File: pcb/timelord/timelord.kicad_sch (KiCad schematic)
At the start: 16 parts, among them J1 Raspberry_Pi_4, J2 OLED, J3 SMA, J4 EXTERNAL, U1 NEO-F10T

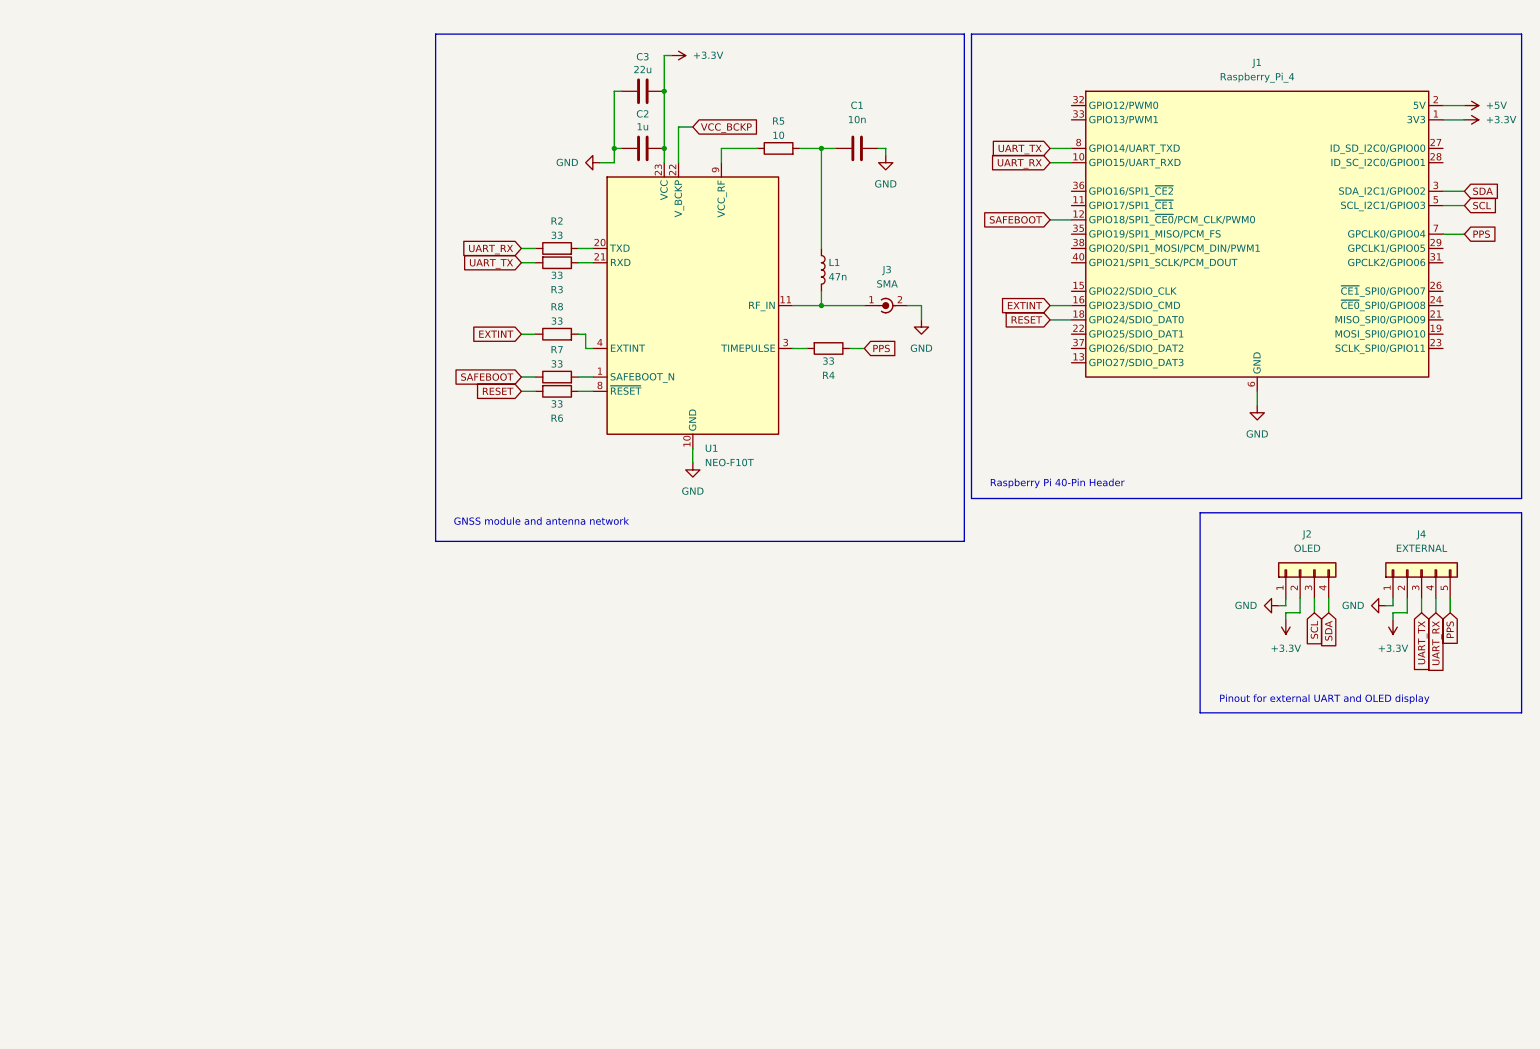
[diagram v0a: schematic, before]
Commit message: Add external I2C RTC
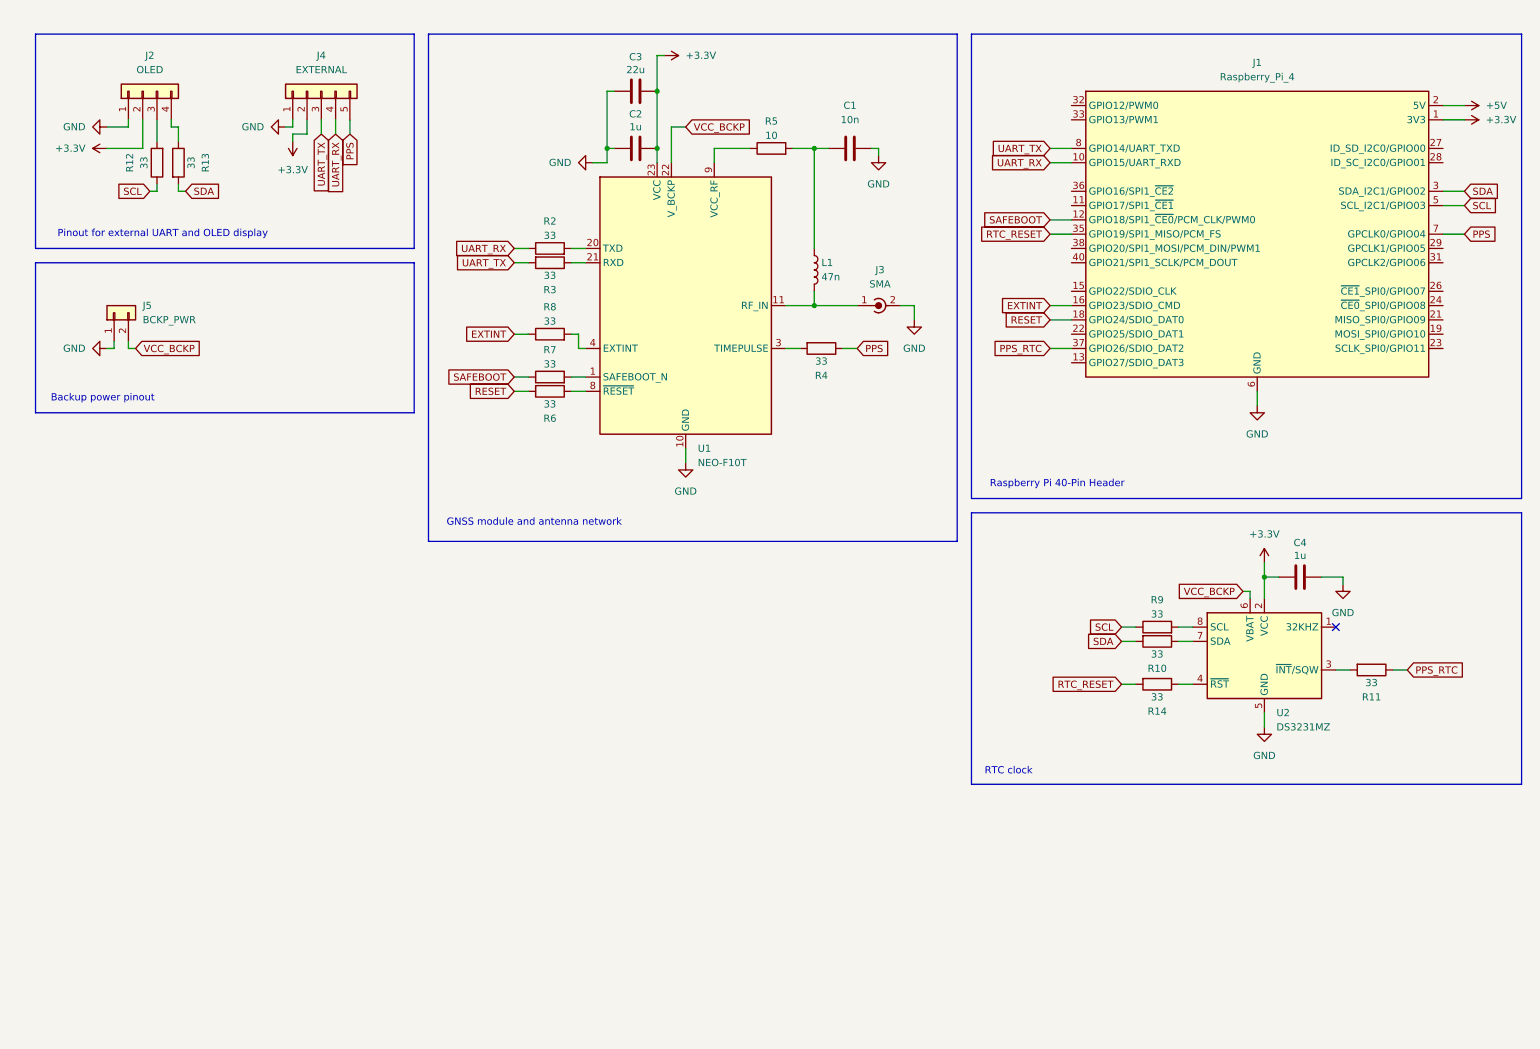
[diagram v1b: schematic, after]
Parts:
- added C4: 1u, Capacitor_SMD:C_0603_1608Metric, symbol Device:C
- added J5: BCKP_PWR, Connector_PinHeader_2.54mm:PinHeader_1x02_P2.54mm_Vertical, symbol Connector_Generic:Conn_01x02
- added R10, R11, R12, R13, R14, R9: 33, Resistor_SMD:R_0603_1608Metric, symbol Device:R
- added U2: DS3231MZ, Package_SO:SOIC-8_3.9x4.9mm_P1.27mm, symbol Timer_RTC:DS3231MZ
- J1: MFR (none) -> 485-2822
- U1: MFR (none) -> 377-NEO-F10T-00B
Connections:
- net +3.3V: now also C4.1, U2.2 (VCC)
- net GND: now also C4.2, J5.1 (Pin_1), U2.5 (GND)
- net SCL: now also R12.1, R9.1; no longer J2.3 (Pin_3)
- net SDA: now also R10.2, R13.2; no longer J2.4 (Pin_4)
- net VCC_BCKP: now also J5.2 (Pin_2), U2.6 (VBAT)
- net RTC_RESET: now reaches J1.35 (GPIO19/SPI1_MISO/PCM_FS)
- net RTC_RESET: now also R14.2
- net PPS_RTC: now reaches J1.37 (GPIO26/SDIO_DAT2)
- net PPS_RTC: now also R11.1
- new net: R11.2, U2.3 (~{INT}/SQW)
- new net: J2.3 (Pin_3), R12.2
- new net: J2.4 (Pin_4), R13.1
- new net: R14.1, U2.4 (~{RST})
- new net: R10.1, U2.7 (SDA)
- new net: R9.2, U2.8 (SCL)
- no-connect marks 0 -> 1
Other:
- note added: "Backup power pinout"
- note added: "RTC clock"
- moved on the sheet: C1, C2, C3, J2, J3, J4, L1, R2, R3, R4, R5, R6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

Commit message: Redesign board edges and add backup power
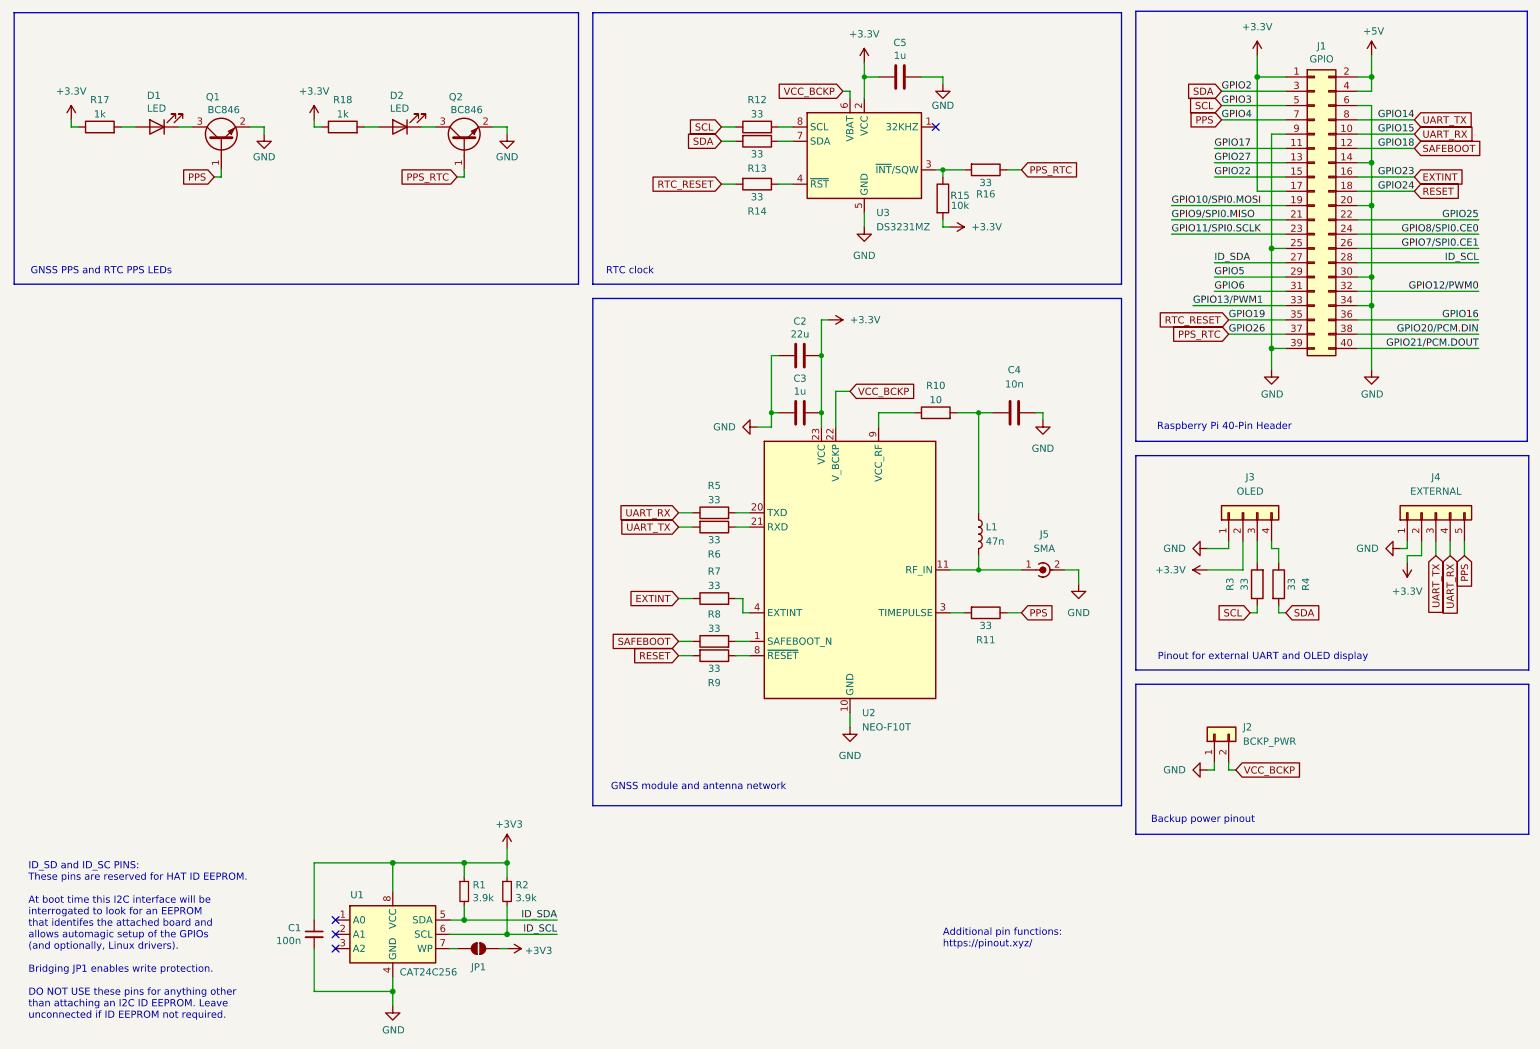
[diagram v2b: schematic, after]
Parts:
- removed J1: Raspberry_Pi_4, Connector_PinSocket_2.54mm:PinSocket_2x20_P2.54mm_Vertical, symbol Connector:Raspberry_Pi_4
- added C1: 100n, symbol Device:C_Small
- added D1, D2: LED, LED_SMD:LED_0603_1608Metric, symbol Device:LED
- added J1: GPIO, Connector_PinSocket_2.54mm:PinSocket_2x20_P2.54mm_Vertical, symbol Connector_Generic:Conn_02x20_Odd_Even
- added JP1: ID_WP, symbol Jumper:SolderJumper_2_Open
- added Q1, Q2: BC846, Package_TO_SOT_SMD:SOT-23, symbol Transistor_BJT:BC846
- added R1, R2: 3.9k, symbol Device:R_Small
- added R15: 10k, Resistor_SMD:R_0805_2012Metric, symbol Device:R
- added R17, R18: 1k, Resistor_SMD:R_0805_2012Metric, symbol Device:R
- added U1: CAT24C256, symbol Memory_EEPROM:CAT24C256
- renumbered C3 to C2, C2 to C3, C1 to C4, C4 to C5, J5 to J2, J2 to J3, J3 to J5, R5 to R10, R4 to R11, R9 to R12, R10 to R13, R11 to R16, R12 to R3, R13 to R4, R2 to R5, R3 to R6, R8 to R7, R7 to R8, R6 to R9, U1 to U2, U2 to U3
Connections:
- net +3.3V: now also J1.1 (Pin_1), J1.17 (Pin_17), R15.2, R17.1, R18.1
- net +5V: now also J1.2 (Pin_2), J1.4 (Pin_4)
- net EXTINT: now also J1.16 (Pin_16)
- net GND: now also C1.2, J1.14 (Pin_14), J1.20 (Pin_20), J1.25 (Pin_25), J1.30 (Pin_30), J1.34 (Pin_34), J1.39 (Pin_39), J1.6 (Pin_6), J1.9 (Pin_9), Q1.2 (E), Q2.2 (E), U1.4 (GND)
- net PPS: now also J1.7 (Pin_7), Q1.1 (B)
- net PPS_RTC: now also J1.37 (Pin_37), Q2.1 (B)
- net RESET: now also J1.18 (Pin_18)
- net RTC_RESET: now also J1.35 (Pin_35)
- net SAFEBOOT: now also J1.12 (Pin_12)
- net SCL: now also J1.5 (Pin_5)
- net SDA: now also J1.3 (Pin_3)
- net UART_RX: now also J1.10 (Pin_10)
- net UART_TX: now also J1.8 (Pin_8)
- net at R16.2, U3.3 (~{INT}/SQW): now also R15.1
- new net: D1.2 (A), R17.2
- new net: JP1.1 (A), U1.7 (WP)
- new net: D1.1 (K), Q1.3 (C)
- new net: D2.1 (K), Q2.3 (C)
- new net: D2.2 (A), R18.2
- new net +3V3: C1.1, JP1.2 (B), R1.1, R2.1, U1.8 (VCC)
- new net GPIO10/SPI0.MOSI: J1.19 (Pin_19)
- new net GPIO11/SPI0.SCLK: J1.23 (Pin_23)
- new net GPIO12/PWM0: J1.32 (Pin_32)
- new net GPIO13/PWM1: J1.33 (Pin_33)
- new net GPIO16: J1.36 (Pin_36)
- new net GPIO17: J1.11 (Pin_11)
- new net GPIO20/PCM.DIN: J1.38 (Pin_38)
- new net GPIO21/PCM.DOUT: J1.40 (Pin_40)
- new net GPIO22: J1.15 (Pin_15)
- new net GPIO25: J1.22 (Pin_22)
- new net GPIO27: J1.13 (Pin_13)
- new net GPIO5: J1.29 (Pin_29)
- new net GPIO6: J1.31 (Pin_31)
- new net GPIO7/SPI0.CE1: J1.26 (Pin_26)
- new net GPIO8/SPI0.CE0: J1.24 (Pin_24)
- new net GPIO9/SPI0.MISO: J1.21 (Pin_21)
- new net ID_SCL: J1.28 (Pin_28), R2.2, U1.6 (SCL)
- new net ID_SDA: J1.27 (Pin_27), R1.2, U1.5 (SDA)
- no-connect marks 1 -> 4
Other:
- note added: "Additional pin functions: https://pinout.xyz/"
- note added: "GNSS PPS and RTC PPS LEDs"
- note added: "ID_SD and ID_SC PINS: These pins are reserved for HAT ID EEPROM. At boot time this I2C interface will be interrogated to look for an EEPROM that identifes the attached board and allows automagic setup of the GPIOs (and optionally, Linux drivers). Bridging JP1 enables write protection. DO NOT USE these pins for anything other than attaching an I2C ID EEPROM. Leave unconnected if ID EEPROM not requ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"
- moved on the sheet: C2, C3, C4, C5, J2, J3, J4, J5, L1, R10, R11, R12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

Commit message: Cosmetic changes
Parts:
- removed C1: 100n, symbol Device:C_Small
- removed R1, R2: 3.9k, symbol Device:R_Small
- removed U1: CAT24C256, symbol Memory_EEPROM:CAT24C256
- JP1: value ID_WP -> VCC_BCPK_JMPR; footprint (none) -> Jumper:SolderJumper-2_P1.3mm_Open_TrianglePad1.0x1.5mm; now left out of the parts list
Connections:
- net +3V3 is gone; now on net VCC_BCKP: JP1.2 (B)
- net +3.3V: now also JP1.1 (A)
- no-connect marks 4 -> 1
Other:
- note added: "GNSS TimeLord RPi Hat"
- note removed: "Additional pin functions: https://pinout.xyz/"
- note removed: "ID_SD and ID_SC PINS: These pins are reserved for HAT ID EEPROM. At boot time this I2C interface will be interrogated to look for an EEPROM that identifes the attached board and allows automagic setup of the GPIOs (and optionally, Linux drivers). Bridging JP1 enables write protection. DO NOT USE these pins for anything other than attaching an I2C ID EEPROM. Leave unconnected if ID EEPROM not requ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"
